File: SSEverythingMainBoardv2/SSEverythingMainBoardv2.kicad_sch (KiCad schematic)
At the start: 64 parts, among them J1 CONN_06SILK_FEMALE_PTH, J2 CONN_06SILK_FEMALE_PTH, J3 POWER, J4 Switch, J5 Conn_01x02, J6 Conn_01x05, M1 Left MOTOR, M2 Right MOTOR, SW1 TACT_SW, U1 DFRobot_DC_Controller

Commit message: updates before complete rearrange
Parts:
- removed C10, C12: 0.1uF, Capacitor_SMD:C_0805_2012Metric_Pad1.18x1.45mm_HandSolder, symbol Device:C
- removed C11, C9: 10uF, Capacitor_SMD:C_0805_2012Metric_Pad1.18x1.45mm_HandSolder, symbol Device:C
- added FET3, FET4: SOT-23 DMG2302UK-7, Package_TO_SOT_SMD:SOT-23_Handsoldering, symbol PB_Library:PMV45EN2
- added R15, R22: 10R, Resistor_SMD:R_0805_2012Metric_Pad1.20x1.40mm_HandSolder, symbol Device:R
- added R16, R23: R56, Resistor_SMD:R_1206_3216Metric_Pad1.30x1.75mm_HandSolder, symbol Device:R
- added TR3, TR4: BC849, Package_TO_SOT_SMD:SOT-23_Handsoldering, symbol Transistor_BJT:BC849
- C1, C2, C3, C5: footprint Capacitor_SMD:C_0805_2012Metric_Pad1.18x1.45mm_HandSolder -> Capacitor_SMD:C_1206_3216Metric_Pad1.33x1.80mm_HandSolder
- C7, C8: value 0.1uF -> 10uF; footprint Capacitor_SMD:C_0805_2012Metric_Pad1.18x1.45mm_HandSolder -> Capacitor_SMD:C_1206_3216Metric_Pad1.33x1.80mm_HandSolder
- FET1, FET2: value PMV45EN2 -> SOT-23 DMG2302UK-7
- R6, R8: footprint Resistor_SMD:R_0805_2012Metric_Pad1.20x1.40mm_HandSolder -> Resistor_SMD:R_1206_3216Metric_Pad1.30x1.75mm_HandSolder
- renumbered FLED1 to FLLED1, FLED2 to FRLED2, DLED1 to LDLED1, DLED2 to RDLED2
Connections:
- net GND: now also C1.1, C2.1, J1.5, J1.6, R16.2, R23.2, TR3.2 (E), TR4.2 (E); no longer C1.2, C2.2, J1.1, J2.1
- net LEFT_ENC_A: now also J2.4; no longer J2.3
- net LEFT_ENC_B: now also J2.3; no longer J2.2
- net LEFT_MOTOR_1: now also J1.1; no longer J2.5
- net LEFT_MOTOR_2: now also J1.2; no longer J2.6
- net RIGHT_ENC_A: now also J2.5; no longer J1.2
- net RIGHT_ENC_B: now also J2.6; no longer J1.3
- net RIGHT_MOTOR_1: now also J1.3; no longer J1.5
- net RIGHT_MOTOR_2: now also J1.4; no longer J1.6
- net Vbatt: now also R15.1, R22.1
- net Vcc: now also J2.1, J2.2; no longer J1.4, J2.4
- net at FET2.1 (G), R2.2, R4.1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: now also FET3.1 (G), TR3.3 (C)
- net at FLLED1.2 (A), R7.2: now also C2.2; no longer C2.1, C7.2
- net at A1.2 (D0/RX): now also R17.2; no longer R17.1
- net at RDLED2.1 (K): now also FET4.3 (D); no longer LDLED1.2 (A)
- net at FRLED2.2 (A): now also C7.2, R15.2; no longer FLLED1.1 (K)
- net at D3.2 (A): now also R17.1; no longer R17.2
- net at FET1.1 (G), R1.2, R3.1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: now also FET4.1 (G), TR4.3 (C)
- net at C8.2, RDLED2.2 (A): now also R22.2; no longer C1.1, R5.2
- net at FRLED2.1 (K): now also FET3.3 (D); no longer FET2.3 (D)
- new net: FET4.2 (S), R23.1, TR4.1 (B)
- new net: FET3.2 (S), R16.1, TR3.1 (B)
- new net: C1.2, LDLED1.2 (A), R5.2
- new net: FET2.3 (D), FLLED1.1 (K)
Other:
- note removed: "LEFT MOTOR"
- note removed: "RIGHT MOTOR"
- moved on the sheet: A1, C1, C2, C3, C5, D3, D4, FET2, FLLED1, FRLED2, J5, J6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

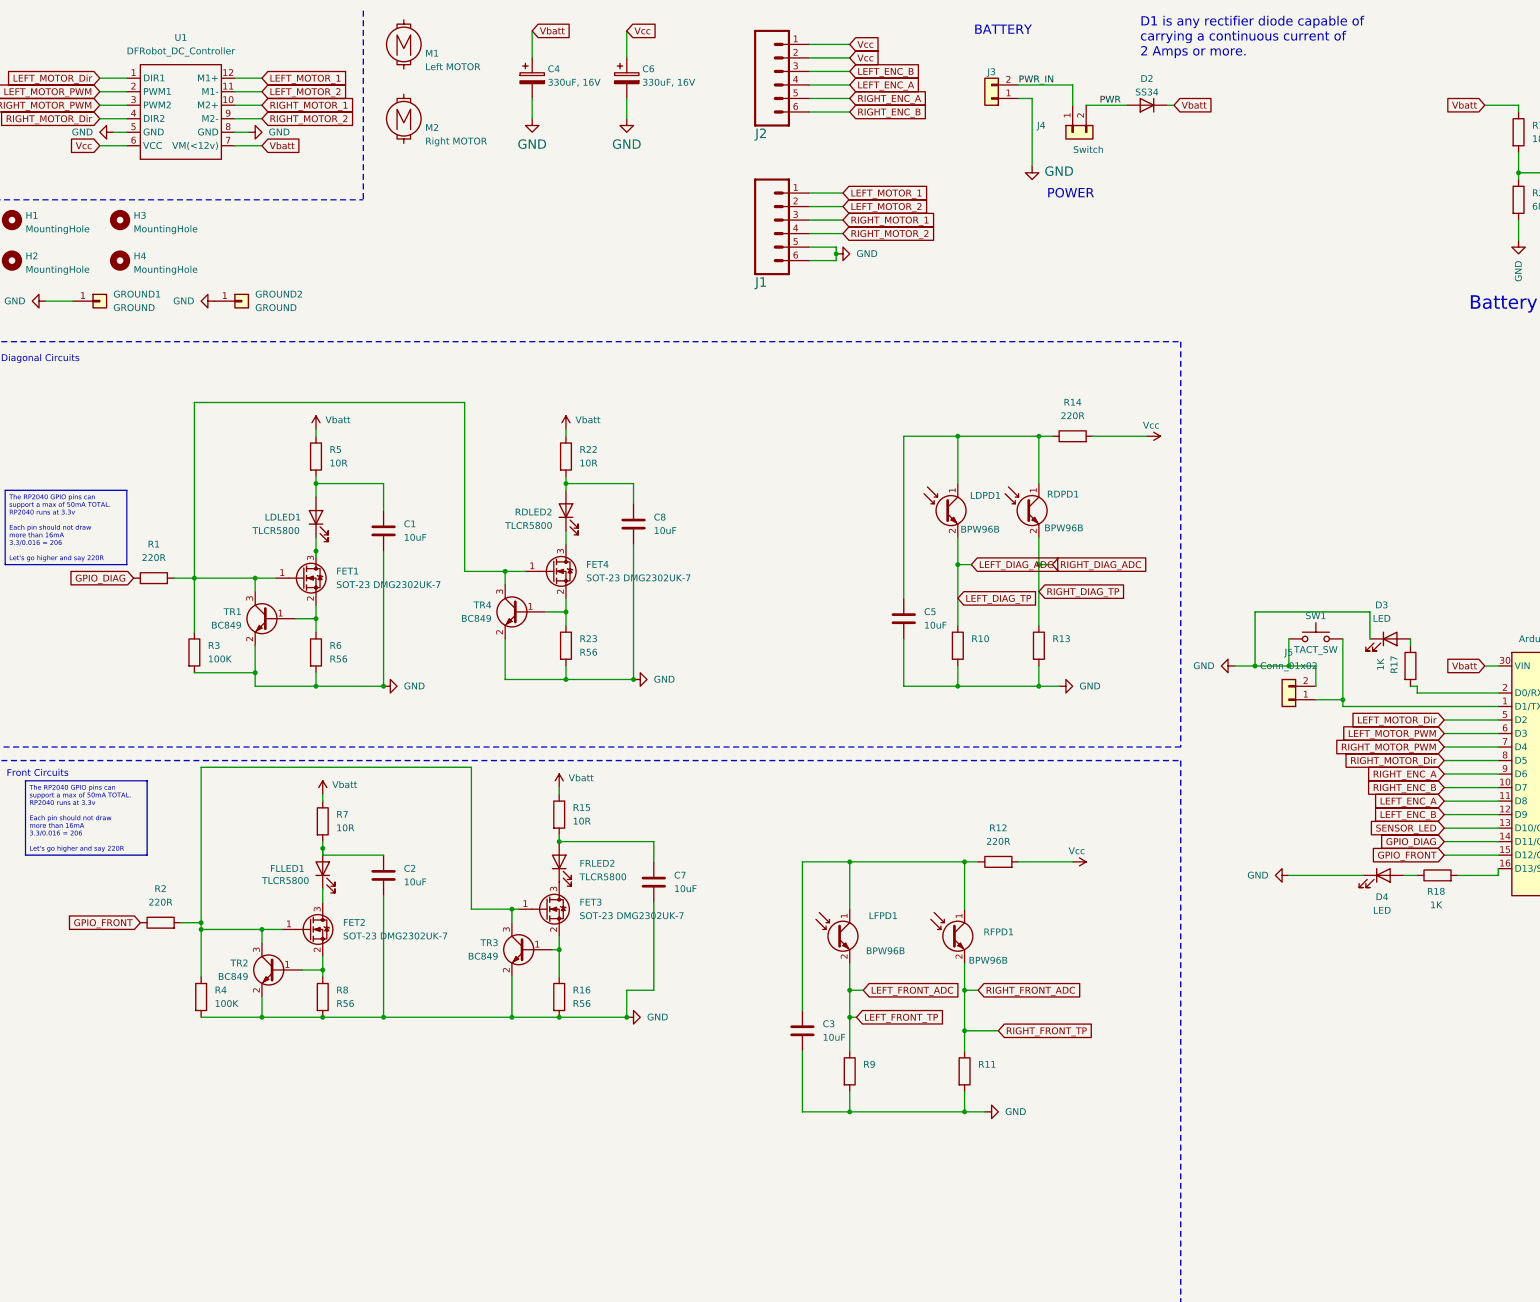
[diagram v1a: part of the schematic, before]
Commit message: before updating to KiCad 9 and changing sensor design
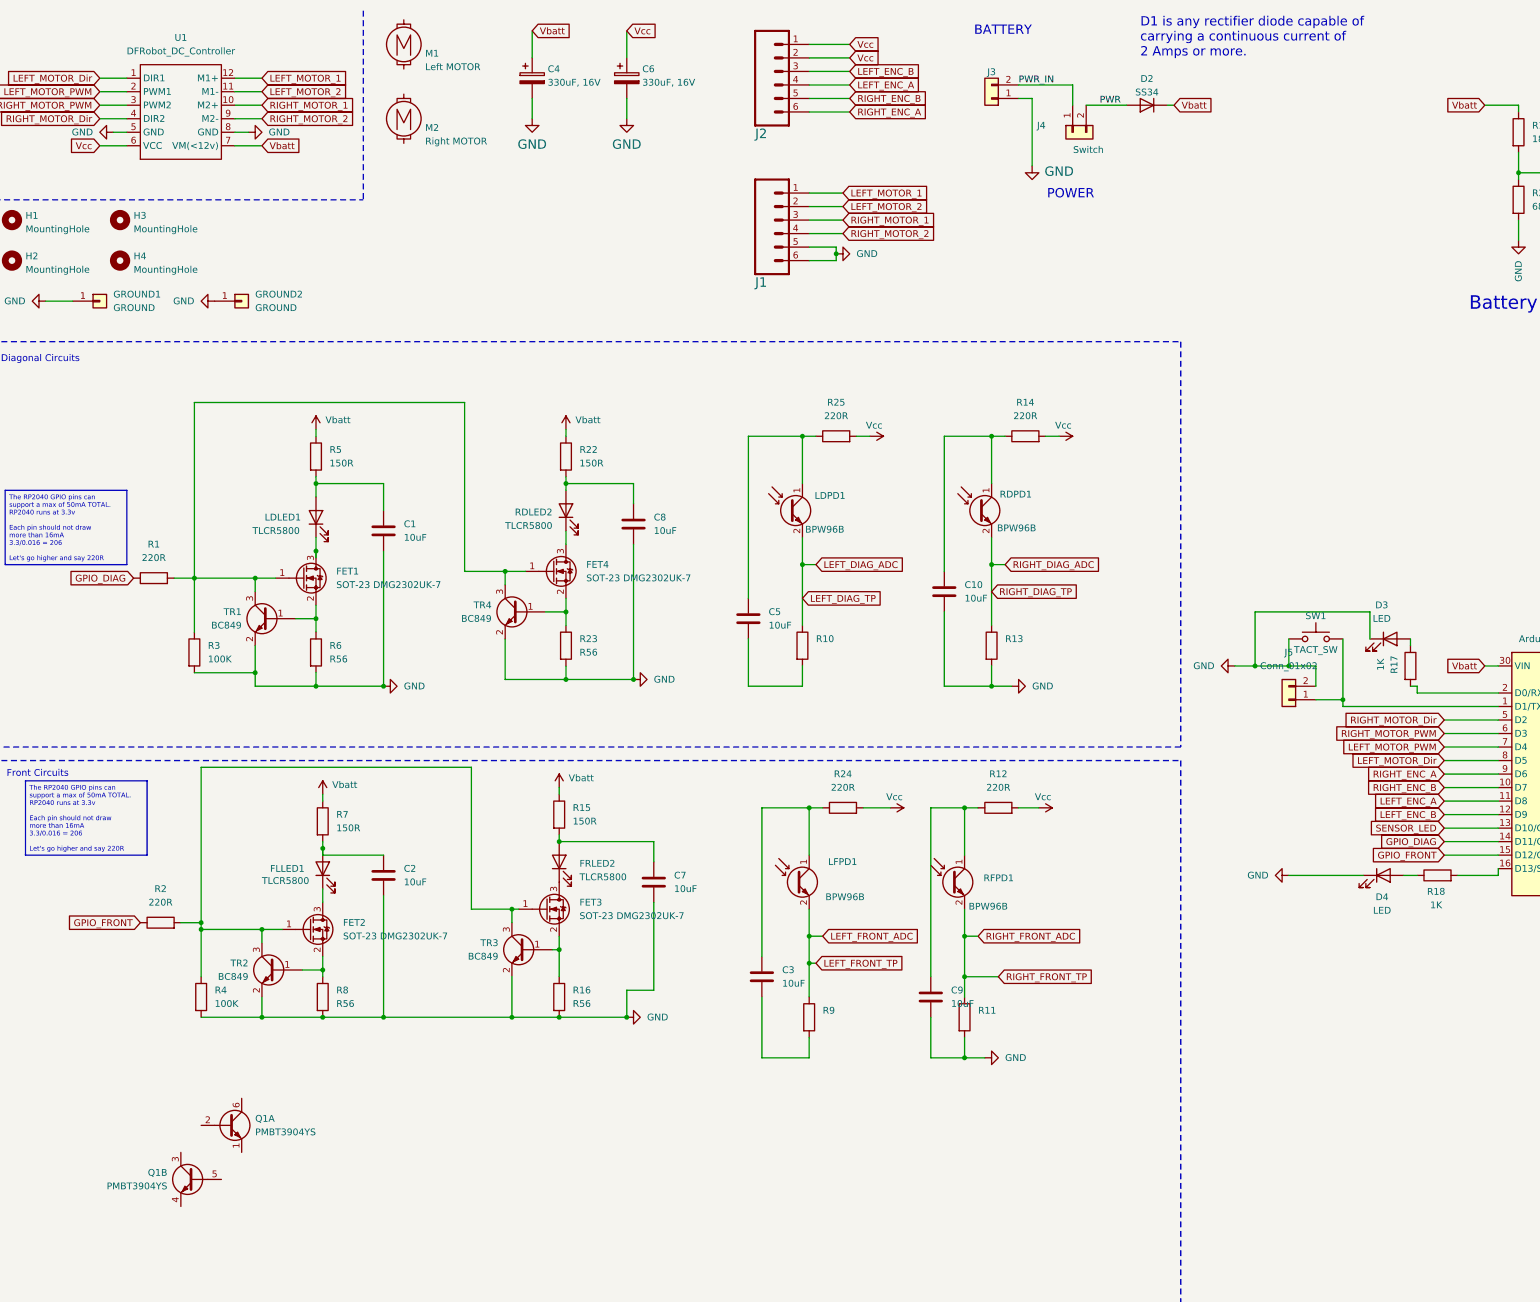
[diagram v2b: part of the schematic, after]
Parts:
- added C10, C9: 10uF, Capacitor_SMD:C_1206_3216Metric_Pad1.33x1.80mm_HandSolder, symbol Device:C
- added Q1: PMBT3904YS, Package_TO_SOT_SMD:SOT-363_SC-70-6, symbol Transistor_BJT:PMBT3904YS
- added R24, R25: 220R, Resistor_SMD:R_0805_2012Metric_Pad1.20x1.40mm_HandSolder, symbol Device:R
- R15, R22, R5, R7: value 10R -> 150R
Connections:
- net GND: now also C10.2, C9.2; no longer C3.2, C5.2, R10.2, R9.2
- net LEFT_MOTOR_Dir: now also A1.8 (D5); no longer A1.5 (D2)
- net LEFT_MOTOR_PWM: now also A1.7 (D4); no longer A1.6 (D3)
- net RIGHT_ENC_A: now also J2.6; no longer J2.5
- net RIGHT_ENC_B: now also J2.5; no longer J2.6
- net RIGHT_MOTOR_Dir: now also A1.5 (D2); no longer A1.8 (D5)
- net RIGHT_MOTOR_PWM: now also A1.6 (D3); no longer A1.7 (D4)
- net Vcc: now also R24.2, R25.2
- net at C3.1, LFPD1.1 (C): now also R24.1; no longer R12.1, RFPD1.1 (C)
- net at C5.1, LDPD1.1 (C): now also R25.1; no longer R14.1, RDPD1.1 (C)
- new net: C3.2, R9.2
- new net: C5.2, R10.2
- new net: C9.1, R12.1, RFPD1.1 (C)
- new net: C10.1, R14.1, RDPD1.1 (C)
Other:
- moved on the sheet: C3, C5, LDPD1, LFPD1, R10, R11, R12, R13, R14, R9, RDPD1, RFPD1

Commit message: first draft of new board all layout complete
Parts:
- removed FET1, FET2, FET3, FET4: SOT-23 DMG2302UK-7, Package_TO_SOT_SMD:SOT-23_Handsoldering, symbol PB_Library:PMV45EN2
- removed R19: 180K, Resistor_SMD:R_0805_2012Metric_Pad1.20x1.40mm_HandSolder, symbol Device:R
- removed R20: 68K, Resistor_SMD:R_0805_2012Metric_Pad1.20x1.40mm_HandSolder, symbol Device:R
- removed TR1, TR2, TR3, TR4: BC849, Package_TO_SOT_SMD:SOT-23_Handsoldering, symbol Transistor_BJT:BC849
- added Q2, Q3, Q4: PBSS4160DS, SamacSys_Parts:SOT95P275X110-6N, symbol Transistor_BJT:PMBT3904YS
- Q1: value PMBT3904YS -> PBSS4160DS; footprint Package_TO_SOT_SMD:SOT-363_SC-70-6 -> SamacSys_Parts:SOT95P275X110-6N
- R1, R2: value 220R -> 1K
- R15, R22, R5, R7: value 150R -> 100R
- R16, R23, R6, R8: value R56 -> 2R
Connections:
- net GND: now also C5.2, Q1.4 (E2), R10.2, R9.2, Q2.4 (E2), Q3.4 (E2), Q4.4 (E2)
- net GPIO_DIAG: now also A1.15 (D12/CIPO); no longer A1.14 (D11/COPI)
- net GPIO_FRONT: now also A1.14 (D11/COPI); no longer A1.15 (D12/CIPO)
- net at R23.1: now also Q4.1 (E1), Q4.5 (B2)
- net at R1.2, R3.1: now also Q3.2 (B1), Q3.3 (C2), Q4.2 (B1), Q4.3 (C2)
- net at R6.1: now also Q3.1 (E1), Q3.5 (B2)
- net at R2.2, R4.1: now also Q1.2 (B1), Q1.3 (C2), Q2.2 (B1), Q2.3 (C2)
- net at LFPD1.1 (C), R24.1: no longer C3.1
- net at C3.2: no longer R9.2
- net at Q1.5 (B2): now also Q1.1 (E1), R8.1
- net at R16.1: now also Q2.1 (E1), Q2.5 (B2)
- net at RDLED2.1 (K): now also Q4.6 (C1)
- net at LDLED1.1 (K): now also Q3.6 (C1)
- net at Q1.6 (C1): now also FLLED1.1 (K)
- net at FRLED2.1 (K): now also Q2.6 (C1)
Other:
- note removed: "Battery Monitor"
- moved on the sheet: C3, Q1A, Q1B

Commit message: First version of v4 board ready for production
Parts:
- M1: footprint ukmarsbot:MINI-METAL-GEARMOTOR-WITH-BRACKET_Alt -> ukmarsbot:MINI-METAL-GEARMOTOR-WITH-BRACKET
- M2: footprint ukmarsbot:MINI-METAL-GEARMOTOR-WITH-BRACKET -> ukmarsbot:MINI-METAL-GEARMOTOR-WITH-BRACKET_Alt
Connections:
- net GND: now also C3.2
- net at C3.1: now also LFPD1.1 (C), R24.1
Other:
- moved on the sheet: C3
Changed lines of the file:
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@@
 	(symbol
 		(lib_id "Device:C")
-		(at 158.75 194.31 90)
+		(at 158.75 194.31 0)
 		(unit 1)
 		(exclude_from_sim no)
@@
 		(fields_autoplaced yes)
 		(property "Reference" "C3"
-			(at 158.75 186.69 90)
+			(at 162.56 193.0399 0)
 			(effects
 				(font
 					(size 1.27 1.27)
 				)
+				(justify left)
 			)
 		)
 		(property "Value" "10uF"
-			(at 158.75 189.23 90)
+			(at 162.56 195.5799 0)
 			(effects
 				(font
 					(size 1.27 1.27)
 				)
+				(justify left)
 			)
 		)
 		(property "Footprint" "Capacitor_SMD:C_1206_3216Metric_Pad1.33x1.80mm_HandSolder"
-			(at 162.56 193.3448 0)
+			(at 159.7152 198.12 0)
 			(effects
 				(font
@@
 			)
 		)
-		(property "Footprint" "ukmarsbot:MINI-METAL-GEARMOTOR-WITH-BRACKET"
+		(property "Footprint" "ukmarsbot:MINI-METAL-GEARMOTOR-WITH-BRACKET_Alt"
 			(at 91.44 34.036 0)
 			(effects
@@
 			)
 		)
-		(property "Footprint" "ukmarsbot:MINI-METAL-GEARMOTOR-WITH-BRACKET_Alt"
+		(property "Footprint" "ukmarsbot:MINI-METAL-GEARMOTOR-WITH-BRACKET"
 			(at 91.44 20.066 0)
 			(effects
